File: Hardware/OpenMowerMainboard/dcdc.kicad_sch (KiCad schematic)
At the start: 24 parts, among them IC3 MAX20405AFOF_VY+T, U1 LM2596S_MODULE

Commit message: update bom error
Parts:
- C15, C18, C19: Digikey 490-1331-1-ND -> 1276-1935-1-ND
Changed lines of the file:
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@@
       (effects (font (size 1.27 1.27)) hide)
     )
-    (property "Digikey" "490-1331-1-ND" (id 4) (at 74.93 104.775 0)
+    (property "Digikey" "1276-1935-1-ND" (id 4) (at 74.93 104.775 0)
       (effects (font (size 1.27 1.27)) hide)
     )
@@
       (effects (font (size 1.27 1.27)) hide)
     )
-    (property "Digikey" "490-1331-1-ND" (id 4) (at 170.815 136.525 0)
+    (property "Digikey" "1276-1935-1-ND" (id 4) (at 170.815 136.525 0)
       (effects (font (size 1.27 1.27)) hide)
     )
@@
       (effects (font (size 1.27 1.27)) hide)
     )
-    (property "Digikey" "490-1331-1-ND" (id 4) (at 183.515 136.525 0)
-      (effects (font (size 1.27 1.27)) hide)
-    )
+    (property "Digikey" "1276-1935-1-ND" (id 4) (at 183.515 136.525 0)
+      (effects (font (size 1.27 1.27)) hide)
+    )

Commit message: BOM changes
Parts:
- C10: value 680uF -> DNP; Config (none) -> do not place; DNP (none) -> Y; Part Number VEJ681M1VTR-1013 -> (none); Stock_PN CP-SMD-680uF-35V -> (none)
- C23, C9: value DNP -> 680uF; Digikey (none) -> 493-9607-2-ND; LCSC (none) -> C882153; Part Number (none) -> VEJ681M1VTR-1013; Stock_PN (none) -> CP-SMD-680uF-35V
- D17, R8: DNP (none) -> Y
- JP4, JP5: DNP (none) -> Y; now left out of the parts list
- U1: value LM2596S_MODULE -> DNP; DNP (none) -> Y
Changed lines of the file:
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@@
       (effects (font (size 1.27 1.27)) (justify left))
     )
-    (property "Value" "DNP" (id 1) (at 31.75 106.4259 0)
+    (property "Value" "680uF" (id 1) (at 31.75 106.4259 0)
       (effects (font (size 1.27 1.27)) (justify left))
     )
@@
       (effects (font (size 1.27 1.27)) hide)
     )
+    (property "LCSC" "C882153" (id 4) (at 28.575 106.045 0)
+      (effects (font (size 1.27 1.27)) hide)
+    )
+    (property "Part Number" "VEJ681M1VTR-1013" (id 5) (at 28.575 106.045 0)
+      (effects (font (size 1.27 1.27)) hide)
+    )
+    (property "Stock_PN" "CP-SMD-680uF-35V" (id 6) (at 28.575 106.045 0)
+      (effects (font (size 1.27 1.27)) hide)
+    )
+    (property "Digikey" "493-9607-2-ND" (id 7) (at 28.575 106.045 0)
+      (effects (font (size 1.27 1.27)) hide)
+    )
     (pin "1")
     (pin "2")
@@
       (effects (font (size 1.27 1.27)) (justify left))
     )
-    (property "Value" "680uF" (id 1) (at 36.83 106.4259 0)
+    (property "Value" "DNP" (id 1) (at 36.83 106.4259 0)
       (effects (font (size 1.27 1.27)) (justify left))
     )
@@
       (effects (font (size 1.27 1.27)) hide)
     )
-    (property "Part Number" "VEJ681M1VTR-1013" (id 5) (at 33.655 106.045 0)
-      (effects (font (size 1.27 1.27)) hide)
-    )
-    (property "Stock_PN" "CP-SMD-680uF-35V" (id 6) (at 33.655 106.045 0)
+    (property "Part Number" "" (id 5) (at 33.655 106.045 0)
+      (effects (font (size 1.27 1.27)) hide)
+    )
+    (property "Stock_PN" "" (id 6) (at 33.655 106.045 0)
+      (effects (font (size 1.27 1.27)) hide)
+    )
+    (property "DNP" "Y" (id 7) (at 33.655 106.045 0)
+      (effects (font (size 1.27 1.27)) hide)
+    )
+    (property "Config" "do not place" (id 8) (at 33.655 106.045 0)
       (effects (font (size 1.27 1.27)) hide)
     )
@@
     )
     (property "Config" "no not place" (id 4) (at 141.605 80.645 0)
+      (effects (font (size 1.27 1.27)) hide)
+    )
+    (property "DNP" "Y" (id 5) (at 141.605 80.645 0)
       (effects (font (size 1.27 1.27)) hide)
     )
@@
   )
   (symbol (lib_id "Jumper:SolderJumper_3_Bridged12") (at 150.495 109.855 270) (mirror x) (unit 1)
-    (in_bom yes) (on_board yes) (fields_autoplaced)
+    (in_bom no) (on_board yes) (fields_autoplaced)
     (property "Reference" "JP4" (id 0) (at 152.4 108.5849 90)
       (effects (font (size 1.27 1.27)) (justify left))
@@
       (effects (font (size 1.27 1.27)) hide)
     )
+    (property "DNP" "Y" (id 5) (at 150.495 109.855 0)
+      (effects (font (size 1.27 1.27)) hide)
+    )
     (pin "1")
     (pin "2")
@@
       (effects (font (size 1.27 1.27)) (justify left))
     )
-    (property "Value" "DNP" (id 1) (at 246.38 136.2709 0)
+    (property "Value" "680uF" (id 1) (at 246.38 136.2709 0)
       (effects (font (size 1.27 1.27)) (justify left))
     )
@@
     )
     (property "Datasheet" "~" (id 3) (at 243.205 135.89 0)
+      (effects (font (size 1.27 1.27)) hide)
+    )
+    (property "LCSC" "C882153" (id 4) (at 243.205 135.89 0)
+      (effects (font (size 1.27 1.27)) hide)
+    )
+    (property "Part Number" "VEJ681M1VTR-1013" (id 5) (at 243.205 135.89 0)
+      (effects (font (size 1.27 1.27)) hide)
+    )
+    (property "Stock_PN" "CP-SMD-680uF-35V" (id 6) (at 243.205 135.89 0)
+      (effects (font (size 1.27 1.27)) hide)
+    )
+    (property "Digikey" "493-9607-2-ND" (id 7) (at 243.205 135.89 0)
       (effects (font (size 1.27 1.27)) hide)
     )
@@
     (in_bom yes) (on_board yes)
     (property "Reference" "U1" (id 0) (at 109.855 24.384 0))
-    (property "Value" "LM2596S_MODULE" (id 1) (at 109.855 26.6954 0))
+    (property "Value" "DNP" (id 1) (at 109.855 26.6954 0))
     (property "Footprint" "MyModules:LM2596S_MODULE" (id 2) (at 110.49 26.035 0)
       (effects (font (size 1.27 1.27)) hide)
@@
     )
     (property "Stock_PN" "U-LM2596SX-5.0" (id 7) (at 110.49 26.035 0)
+      (effects (font (size 1.27 1.27)) hide)
+    )
+    (property "DNP" "Y" (id 8) (at 110.49 26.035 0)
       (effects (font (size 1.27 1.27)) hide)
     )
@@
   )
   (symbol (lib_id "Jumper:SolderJumper_3_Bridged12") (at 158.115 99.695 270) (mirror x) (unit 1)
-    (in_bom yes) (on_board yes) (fields_autoplaced)
+    (in_bom no) (on_board yes) (fields_autoplaced)
     (property "Reference" "JP5" (id 0) (at 160.02 98.4249 90)
       (effects (font (size 1.27 1.27)) (justify left))
@@
     )
     (property "Config" "do not place" (id 4) (at 158.115 99.695 0)
+      (effects (font (size 1.27 1.27)) hide)
+    )
+    (property "DNP" "Y" (id 5) (at 158.115 99.695 0)
       (effects (font (size 1.27 1.27)) hide)
     )
@@
       (effects (font (size 1.27 1.27)) hide)
     )
+    (property "DNP" "Y" (id 5) (at 186.69 115.57 0)
+      (effects (font (size 1.27 1.27)) hide)
+    )

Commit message: fixed BOM
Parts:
- C23, C9: Digikey 493-9607-2-ND -> P124828TR-ND
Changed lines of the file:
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@@
       (effects (font (size 1.27 1.27)) hide)
     )
-    (property "Digikey" "493-9607-2-ND" (id 7) (at 28.575 106.045 0)
+    (property "Digikey" "P124828TR-ND" (id 7) (at 28.575 106.045 0)
       (effects (font (size 1.27 1.27)) hide)
     )
@@
       (effects (font (size 1.27 1.27)) hide)
     )
-    (property "Digikey" "493-9607-2-ND" (id 7) (at 243.205 135.89 0)
+    (property "Digikey" "P124828TR-ND" (id 7) (at 243.205 135.89 0)
       (effects (font (size 1.27 1.27)) hide)
     )

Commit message: feat(bom): added compatible lcsc codes, updated discontinued ones
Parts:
- C23, C9: LCSC C882153 -> C2980172; Part Number VEJ681M1VTR-1013 -> GVM1V681M1010
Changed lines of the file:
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@@
       (effects (font (size 1.27 1.27)) hide)
     )
-    (property "LCSC" "C882153" (id 4) (at 28.575 106.045 0)
+    (property "LCSC" "C2980172" (id 4) (at 28.575 106.045 0)
       (effects (font (size 1.27 1.27)) hide)
     )
-    (property "Part Number" "VEJ681M1VTR-1013" (id 5) (at 28.575 106.045 0)
+    (property "Part Number" "GVM1V681M1010" (id 5) (at 28.575 106.045 0)
       (effects (font (size 1.27 1.27)) hide)
     )
@@
       (effects (font (size 1.27 1.27)) hide)
     )
-    (property "LCSC" "C882153" (id 4) (at 243.205 135.89 0)
+    (property "LCSC" "C2980172" (id 4) (at 243.205 135.89 0)
       (effects (font (size 1.27 1.27)) hide)
     )
-    (property "Part Number" "VEJ681M1VTR-1013" (id 5) (at 243.205 135.89 0)
+    (property "Part Number" "GVM1V681M1010" (id 5) (at 243.205 135.89 0)
       (effects (font (size 1.27 1.27)) hide)
     )

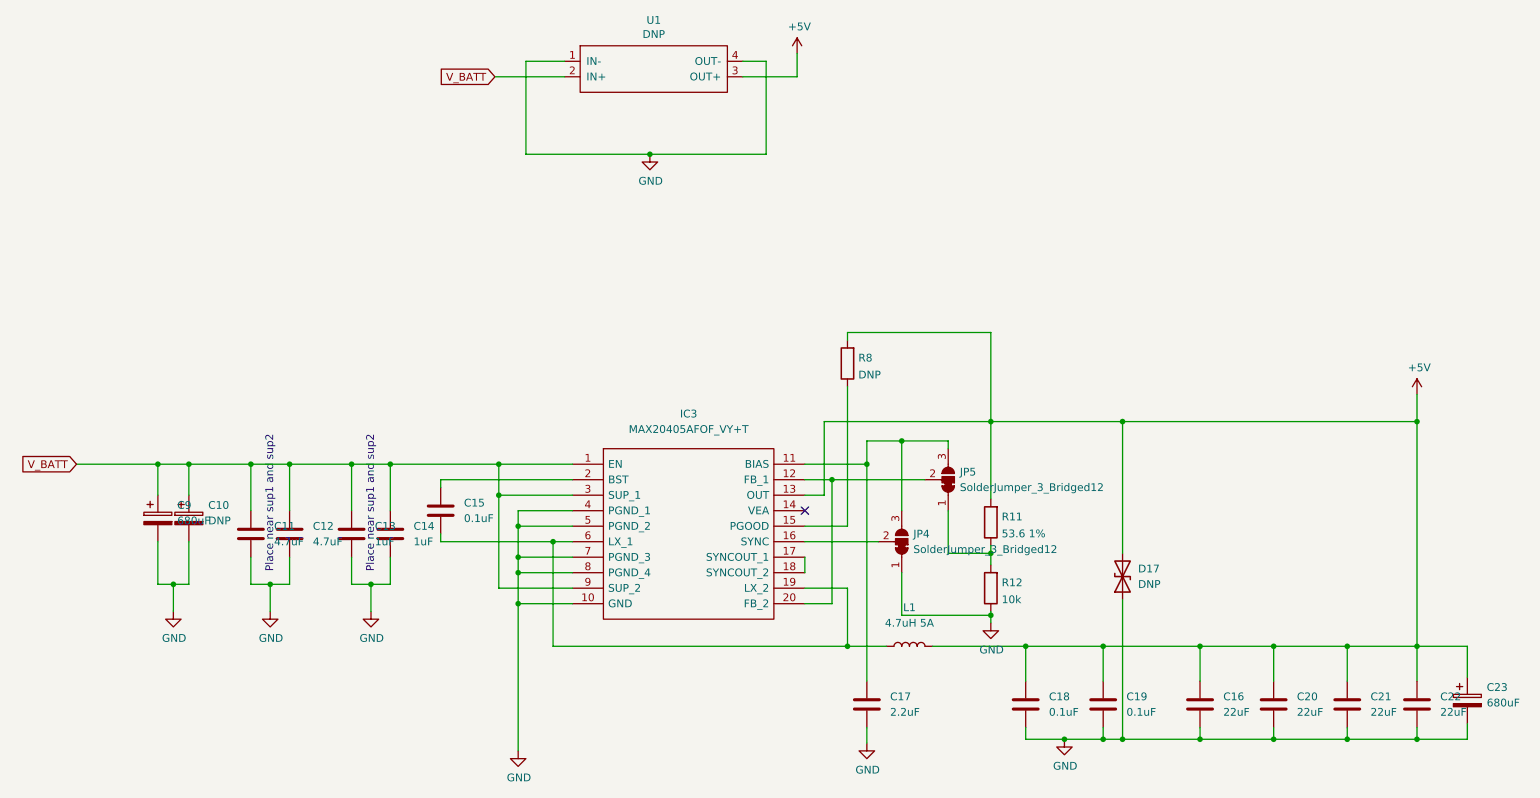
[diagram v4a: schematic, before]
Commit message: fix: fixed ERC/DRC errors, removed LM2596S
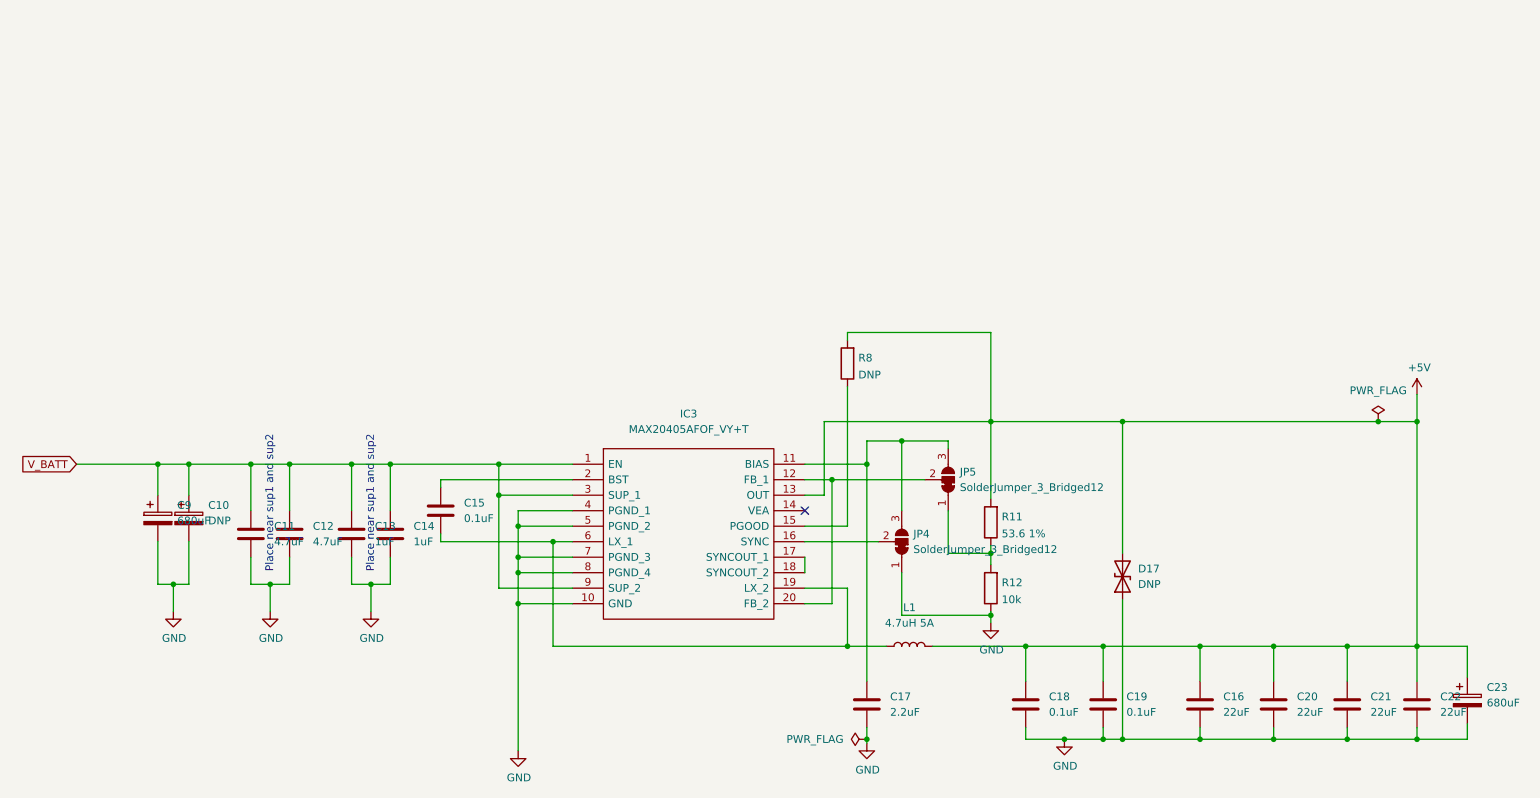
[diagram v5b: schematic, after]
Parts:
- removed U1: DNP, MyModules:LM2596S_MODULE, symbol MyModules:LM2596S_MODULE
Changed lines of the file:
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@@
   (junction (at 183.515 142.24) (diameter 0) (color 0 0 0 0)
   )
-  (junction (at 109.22 46.355) (diameter 0) (color 0 0 0 0)
-  )
   (junction (at 223.52 127) (diameter 0) (color 0 0 0 0)
   )
@@
   (junction (at 177.165 142.24) (diameter 0) (color 0 0 0 0)
   )
+  (junction (at 228.6 90.17) (diameter 0) (color 0 0 0 0)
+  )
   (junction (at 211.455 142.24) (diameter 0) (color 0 0 0 0)
   )
@@
   )
   (junction (at 165.1 90.17) (diameter 0) (color 0 0 0 0)
+  )
+  (junction (at 144.78 142.24) (diameter 0) (color 0 0 0 0)
   )
   (junction (at 33.655 97.155) (diameter 0) (color 0 0 0 0)
@@
     (stroke (width 0) (type default) (color 0 0 0 0))
   )
-  (wire (pts (xy 83.82 33.655) (xy 95.25 33.655))
-    (stroke (width 0) (type default) (color 0 0 0 0))
-  )
   (wire (pts (xy 50.165 112.395) (xy 50.165 116.84))
     (stroke (width 0) (type default) (color 0 0 0 0))
@@
     (stroke (width 0) (type default) (color 0 0 0 0))
   )
-  (wire (pts (xy 133.35 33.655) (xy 133.35 29.845))
-    (stroke (width 0) (type default) (color 0 0 0 0))
-  )
   (wire (pts (xy 211.455 142.24) (xy 199.39 142.24))
     (stroke (width 0) (type default) (color 0 0 0 0))
   )
-  (wire (pts (xy 186.69 90.17) (xy 234.95 90.17))
+  (wire (pts (xy 186.69 90.17) (xy 228.6 90.17))
     (stroke (width 0) (type default) (color 0 0 0 0))
   )
@@
     (stroke (width 0) (type default) (color 0 0 0 0))
   )
-  (wire (pts (xy 128.27 31.115) (xy 128.27 46.355))
-    (stroke (width 0) (type default) (color 0 0 0 0))
-  )
   (wire (pts (xy 60.325 112.395) (xy 60.325 116.84))
     (stroke (width 0) (type default) (color 0 0 0 0))
@@
     (stroke (width 0) (type default) (color 0 0 0 0))
   )
-  (wire (pts (xy 124.46 31.115) (xy 128.27 31.115))
-    (stroke (width 0) (type default) (color 0 0 0 0))
-  )
   (wire (pts (xy 87.63 114.935) (xy 96.52 114.935))
     (stroke (width 0) (type default) (color 0 0 0 0))
@@
     (stroke (width 0) (type default) (color 0 0 0 0))
   )
-  (wire (pts (xy 124.46 33.655) (xy 133.35 33.655))
-    (stroke (width 0) (type default) (color 0 0 0 0))
-  )
   (wire (pts (xy 183.515 142.24) (xy 183.515 140.335))
     (stroke (width 0) (type default) (color 0 0 0 0))
@@
     (stroke (width 0) (type default) (color 0 0 0 0))
   )
-  (wire (pts (xy 88.9 31.115) (xy 88.9 46.355))
-    (stroke (width 0) (type default) (color 0 0 0 0))
-  )
   (wire (pts (xy 93.345 109.855) (xy 93.345 127))
     (stroke (width 0) (type default) (color 0 0 0 0))
@@
     (stroke (width 0) (type default) (color 0 0 0 0))
   )
-  (wire (pts (xy 109.22 46.355) (xy 88.9 46.355))
-    (stroke (width 0) (type default) (color 0 0 0 0))
-  )
   (wire (pts (xy 28.575 116.84) (xy 31.115 116.84))
     (stroke (width 0) (type default) (color 0 0 0 0))
   )
-  (wire (pts (xy 128.27 46.355) (xy 109.22 46.355))
-    (stroke (width 0) (type default) (color 0 0 0 0))
-  )
-  (wire (pts (xy 144.78 140.335) (xy 144.78 142.875))
+  (wire (pts (xy 144.78 140.335) (xy 144.78 142.24))
     (stroke (width 0) (type default) (color 0 0 0 0))
   )
@@
     (stroke (width 0) (type default) (color 0 0 0 0))
   )
-  (wire (pts (xy 95.25 31.115) (xy 88.9 31.115))
-    (stroke (width 0) (type default) (color 0 0 0 0))
-  )
   (wire (pts (xy 33.655 116.84) (xy 33.655 109.855))
     (stroke (width 0) (type default) (color 0 0 0 0))
@@
     (stroke (width 0) (type default) (color 0 0 0 0))
   )
+  (wire (pts (xy 144.78 142.24) (xy 144.78 142.875))
+    (stroke (width 0) (type default) (color 0 0 0 0))
+  )
   (wire (pts (xy 87.63 104.775) (xy 87.63 107.315))
     (stroke (width 0) (type default) (color 0 0 0 0))
@@
   )
   (wire (pts (xy 66.675 97.155) (xy 66.675 104.775))
+    (stroke (width 0) (type default) (color 0 0 0 0))
+  )
+  (wire (pts (xy 228.6 90.17) (xy 234.95 90.17))
     (stroke (width 0) (type default) (color 0 0 0 0))
   )
@@
     )
   )
-  (global_label "V_BATT" (shape input) (at 83.82 33.655 180) (fields_autoplaced)
-    (effects (font (size 1.27 1.27)) (justify right))
-    (property "Intersheet References" "${INTERSHEET_REFS}" (id 0) (at 75.1458 33.7344 0)
-      (effects (font (size 1.27 1.27)) (justify right) hide)
-    )
-  )
   (symbol (lib_id "Device:C") (at 74.93 104.775 0) (unit 1)
     (in_bom yes) (on_board yes) (fields_autoplaced)
@@
     (pin "2")
   )
+  (symbol (lib_id "power:PWR_FLAG") (at 228.6 90.17 0) (unit 1)
+    (in_bom yes) (on_board yes) (fields_autoplaced)
+    (property "Reference" "#FLG0102" (id 0) (at 228.6 88.265 0)
+      (effects (font (size 1.27 1.27)) hide)
+    )
+    (property "Value" "PWR_FLAG" (id 1) (at 228.6 85.09 0))
+    (property "Footprint" "" (id 2) (at 228.6 90.17 0)
+      (effects (font (size 1.27 1.27)) hide)
+    )
+    (property "Datasheet" "~" (id 3) (at 228.6 90.17 0)
+      (effects (font (size 1.27 1.27)) hide)
+    )
+    (pin "1")
+  )
   (symbol (lib_id "Jumper:SolderJumper_3_Bridged12") (at 150.495 109.855 270) (mirror x) (unit 1)
     (in_bom no) (on_board yes) (fields_autoplaced)
@@
     (pin "1")
     (pin "2")
-  )
-  (symbol (lib_id "MyModules:LM2596S_MODULE") (at 110.49 26.035 180) (unit 1)
-    (in_bom yes) (on_board yes)
-    (property "Reference" "U1" (id 0) (at 109.855 24.384 0))
-    (property "Value" "DNP" (id 1) (at 109.855 26.6954 0))
-    (property "Footprint" "MyModules:LM2596S_MODULE" (id 2) (at 110.49 26.035 0)
-      (effects (font (size 1.27 1.27)) hide)
-    )
-    (property "Datasheet" "" (id 3) (at 110.49 26.035 0)
-      (effects (font (size 1.27 1.27)) hide)
-    )
-    (property "Config" "bench_test" (id 4) (at 110.49 26.035 0)
-      (effects (font (size 1.27 1.27)) hide)
-    )
-    (property "Digikey" "LM2596SX-5.0/NOPBCT-ND" (id 5) (at 110.49 26.035 0)
-      (effects (font (size 1.27 1.27)) hide)
-    )
-    (property "Part Number" "LM2596SX-5.0/NOPB" (id 6) (at 110.49 26.035 0)
-      (effects (font (size 1.27 1.27)) hide)
-    )
-    (property "Stock_PN" "U-LM2596SX-5.0" (id 7) (at 110.49 26.035 0)
-      (effects (font (size 1.27 1.27)) hide)
-    )
-    (property "DNP" "Y" (id 8) (at 110.49 26.035 0)
-      (effects (font (size 1.27 1.27)) hide)
-    )
-    (pin "1")
-    (pin "2")
-    (pin "3")
-    (pin "4")
   )
   (symbol (lib_id "Device:C") (at 199.39 136.525 0) (unit 1)
@@
     (pin "2")
   )
-  (symbol (lib_id "power:+5V") (at 133.35 29.845 0) (unit 1)
-    (in_bom yes) (on_board yes)
-    (property "Reference" "#PWR0107" (id 0) (at 133.35 33.655 0)
-      (effects (font (size 1.27 1.27)) hide)
-    )
-    (property "Value" "+5V" (id 1) (at 133.731 25.4508 0))
-    (property "Footprint" "" (id 2) (at 133.35 29.845 0)
-      (effects (font (size 1.27 1.27)) hide)
-    )
-    (property "Datasheet" "" (id 3) (at 133.35 29.845 0)
-      (effects (font (size 1.27 1.27)) hide)
-    )
-    (pin "1")
-  )
   (symbol (lib_id "Device:C") (at 50.165 108.585 0) (unit 1)
     (in_bom yes) (on_board yes) (fields_autoplaced)
@@
     (pin "1")
     (pin "2")
-  )
-  (symbol (lib_id "power:GND") (at 109.22 46.355 0) (unit 1)
-    (in_bom yes) (on_board yes)
-    (property "Reference" "#PWR0106" (id 0) (at 109.22 52.705 0)
-      (effects (font (size 1.27 1.27)) hide)
-    )
-    (property "Value" "GND" (id 1) (at 109.347 50.7492 0))
-    (property "Footprint" "" (id 2) (at 109.22 46.355 0)
-      (effects (font (size 1.27 1.27)) hide)
-    )
-    (property "Datasheet" "" (id 3) (at 109.22 46.355 0)
-      (effects (font (size 1.27 1.27)) hide)
-    )
-    (pin "1")
   )
   (symbol (lib_id "power:GND") (at 63.5 121.285 0) (unit 1)
@@
       (effects (font (size 1.27 1.27)) hide)
     )
+    (pin "1")
+  )
+  (symbol (lib_id "power:PWR_FLAG") (at 144.78 142.24 90) (unit 1)
+    (in_bom yes) (on_board yes) (fields_autoplaced)
+    (property "Reference" "#FLG0101" (id 0) (at 142.875 142.24 0)
+      (effects (font (size 1.27 1.27)) hide)
+    )
+    (property "Value" "PWR_FLAG" (id 1) (at 140.97 142.2399 90)
+      (effects (font (size 1.27 1.27)) (justify left))
+    )
+    (property "Footprint" "" (id 2) (at 144.78 142.24 0)
+      (effects (font (size 1.27 1.27)) hide)
+    )
+    (property "Datasheet" "~" (id 3) (at 144.78 142.24 0)
+      (effects (font (size 1.27 1.27)) hide)
+    )
